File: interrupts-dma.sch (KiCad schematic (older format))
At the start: 6 parts, among them IC13 74LS373, IC14 8259A, IC19 74LS670, IC34 8237, IC52 74LS04

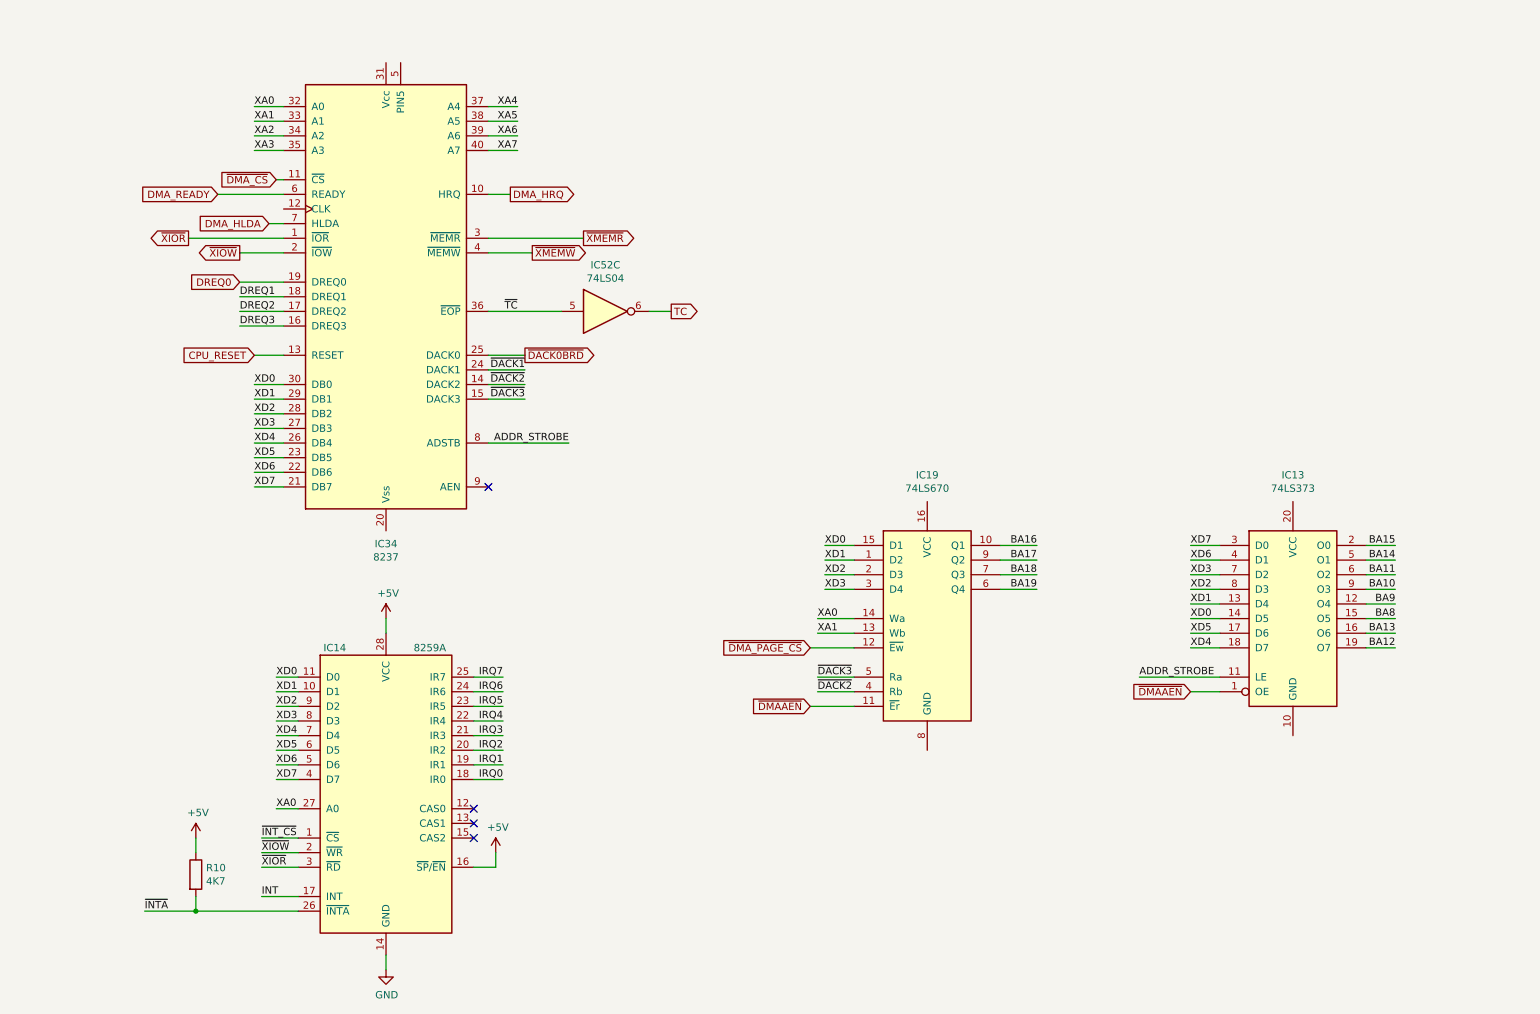
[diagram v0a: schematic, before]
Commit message: Tidy up and map all signals
This fixes up the schematic to:
 - Look presentable
 - Fix all labels connecting sheets
 - Tidy up all loose ends by either inspecting the PCB under
    magnification, measuring with an oscillosope or buzzing
    out with a meter
 - Pass ERC (with 1 exception due to incorrect circuitry around
    pin 33 on the FPU (~RQ~/~GT1~)
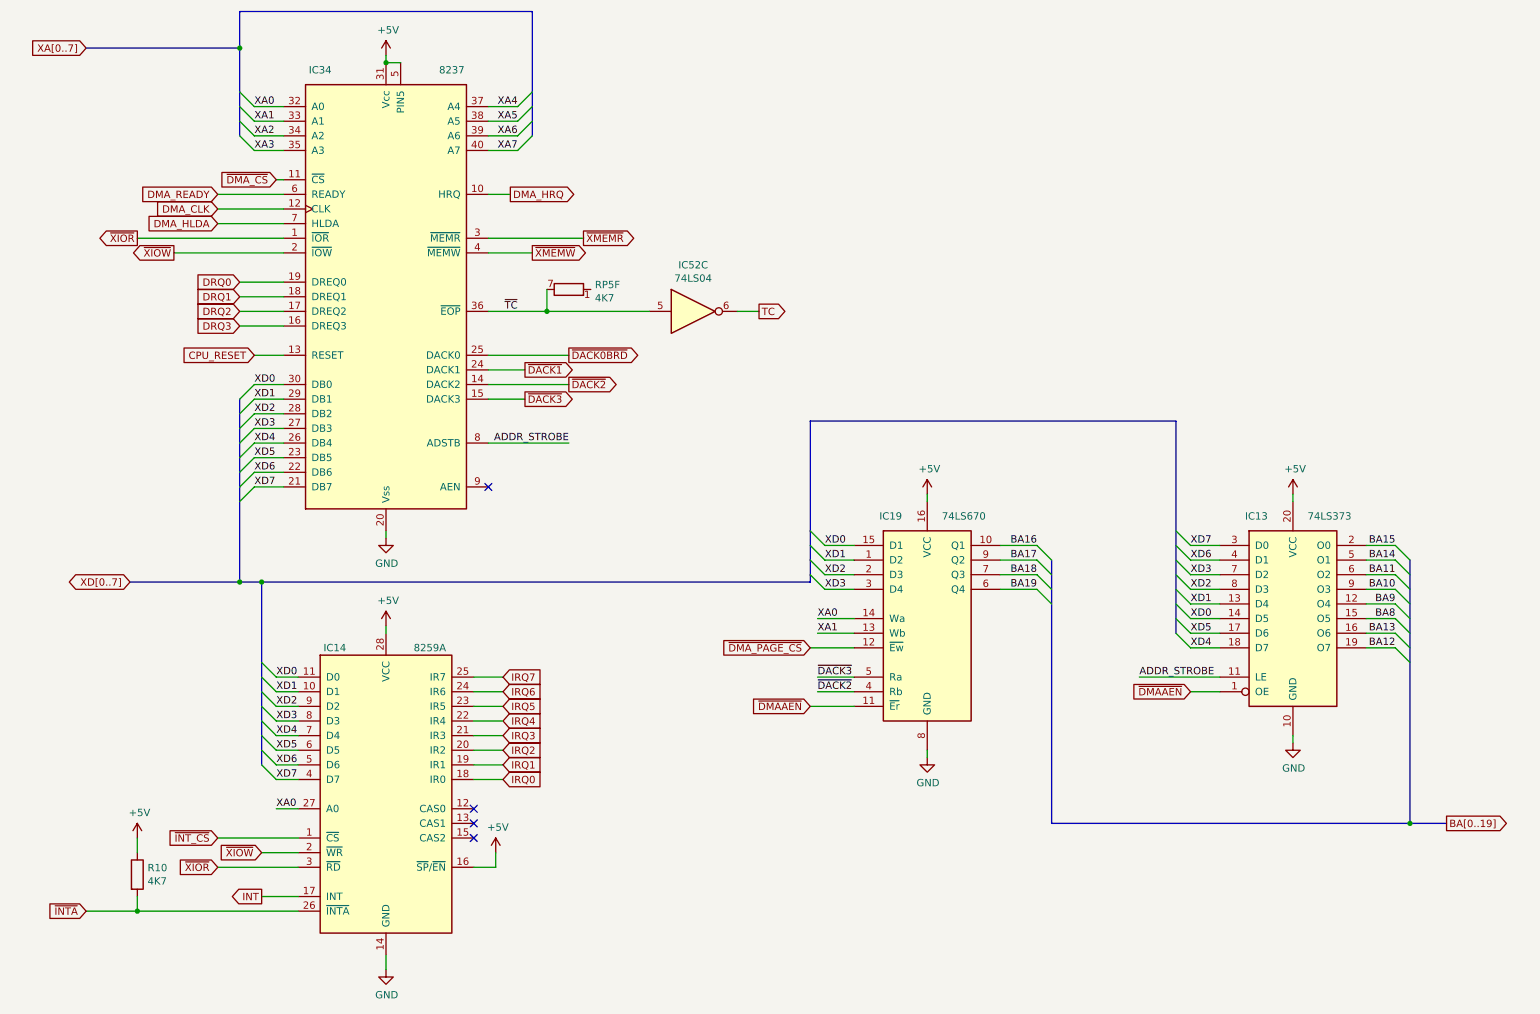
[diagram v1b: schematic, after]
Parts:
- added RP5: 4K7, Resistor_THT:R_Array_SIP9, symbol Device:R_Network08_Split
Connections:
- net +5V: now also IC13.20 (VCC), IC19.16 (VCC), IC34.31 (Vcc), IC34.5 (PIN5)
- net GND: now also IC13.10 (GND), IC19.8 (GND), IC34.20 (Vss)
- net ~TC~: now also RP5.7 (R6.2)
- net DMA_CLK: now reaches IC34.12 (CLK)
- net DREQ0 renamed DRQ0
- net DREQ1 renamed DRQ1
- net DREQ2 renamed DRQ2
- net DREQ3 renamed DRQ3
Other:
- moved on the sheet: IC52C, R10
